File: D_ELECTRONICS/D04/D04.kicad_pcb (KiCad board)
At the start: 2 copper layers, 27.9 x 48.3 mm, 22 parts, among them J0 Conn_01x01_Male, J1 Conn_01x01_Male, J2 Conn_01x01_Male, J3 Conn_01x01_Male, J4 Conn_01x03_Female, J5 Conn_01x04_Female, K1 G5LE-1, Q1 MMBT3904, U2 LTV-817S

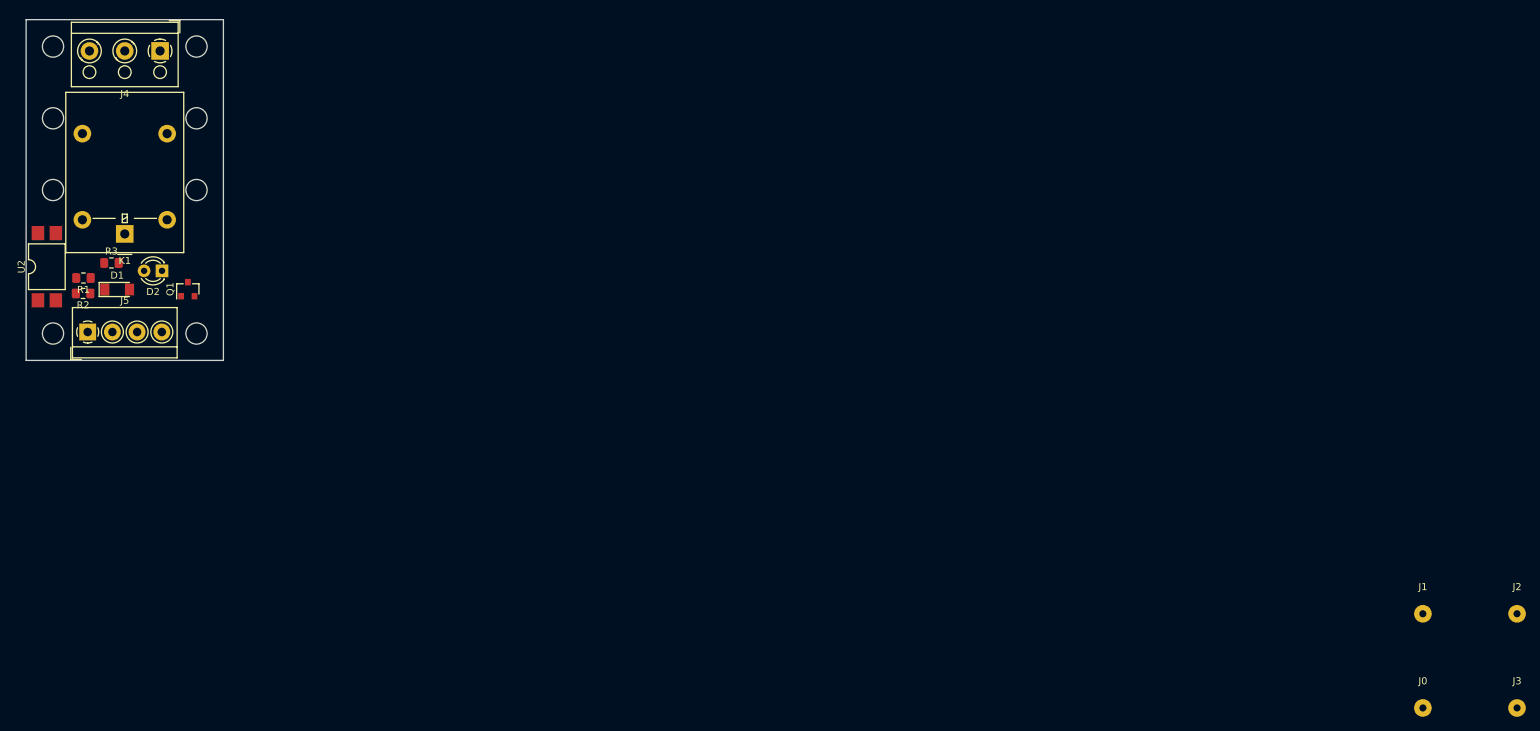
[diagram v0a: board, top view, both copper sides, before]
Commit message: all traces routed
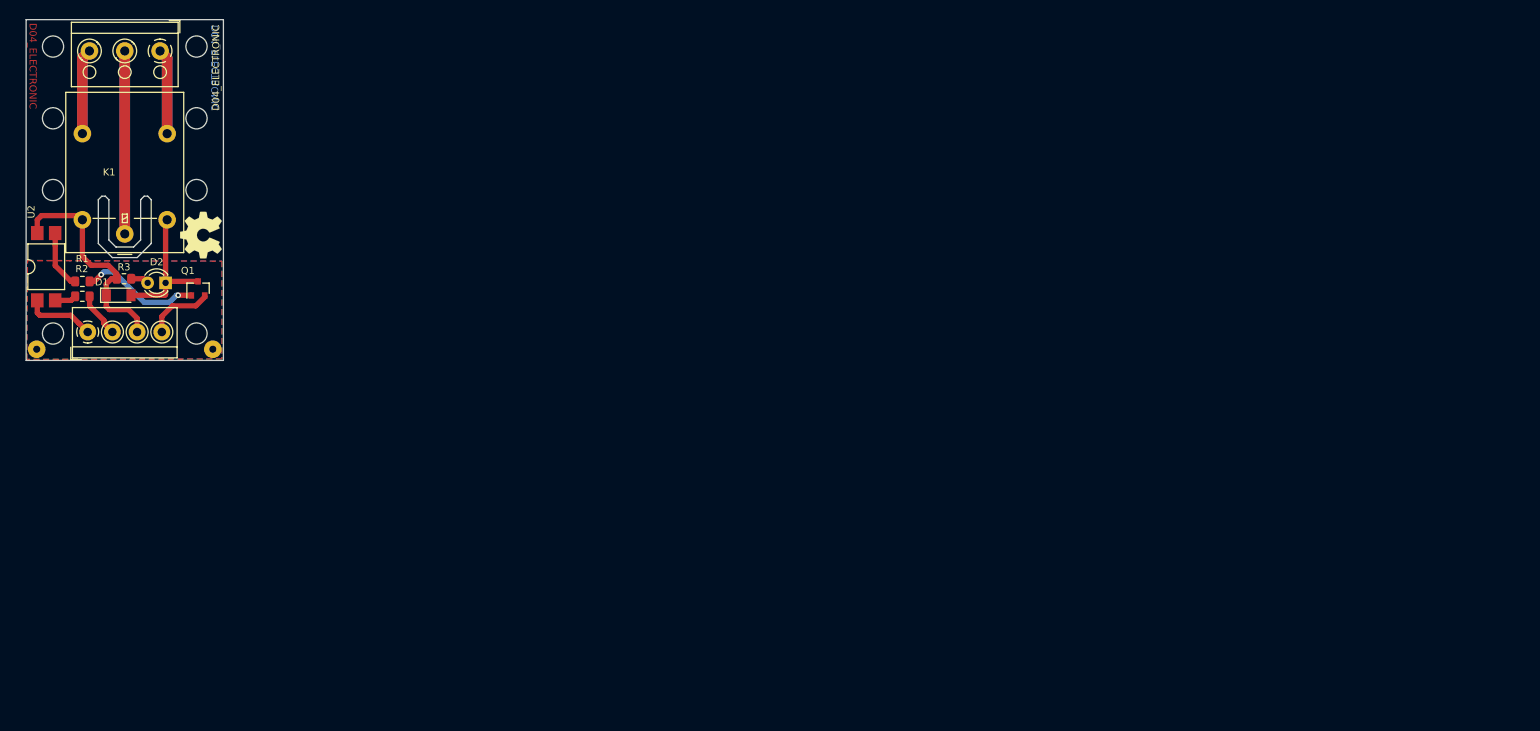
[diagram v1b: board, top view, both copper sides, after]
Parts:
- removed J2, J3: Conn_01x01_Male, Connector_Wire:SolderWirePad_1x01_Drill1mm
- added REF**: OSHW-Symbol_6.7x6mm_SilkScreen, Symbol:OSHW-Symbol_6.7x6mm_SilkScreen, B.Cu at (23.6, 54.3)
- added REF**: OSHW-Symbol_6.7x6mm_SilkScreen, Symbol:OSHW-Symbol_6.7x6mm_SilkScreen, F.Cu at (44.8, 50.5)
- moved J0 202.8 mm to (21.5, 66.7), turned to 45 degrees
- moved J1 175.4 mm to (46.4, 66.7), turned to 45 degrees
- moved R3 2.86 mm to (33.9, 56.7)
- moved D2 1.78 mm to (39.8, 57.3)
- moved Q1 1.45 mm to (44.3, 58.1)
- moved D1 0.84 mm to (33.1, 59.0)
- moved R1 0.51 mm to (28.0, 57.1)
- moved R2 0.42 mm to (28.0, 59.2)
- moved U2 0.09 mm to (22.9, 55.0)
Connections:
- J5 pad 1: Net-(D1-Pad1) -> Net-(J5-Pad1)
- J5 pad 3: Net-(J5-Pad3) -> Net-(D1-Pad1)
- R2 pad 1: Net-(R2-Pad1) -> Net-(J5-Pad2)
- U2 pad 1: Net-(R2-Pad2) -> Net-(J5-Pad1)
- U2 pad 2: Net-(U2-Pad2) -> Net-(R2-Pad2)
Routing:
- net Net-(J4-Pad2): track 0.00 -> 51.8 mm
- net Net-(D1-Pad1): track 0.00 -> 32.5 mm
- net Net-(J4-Pad3): track 0.00 -> 24.2 mm
- net Net-(J4-Pad1): track 0.00 -> 24.2 mm
- net Net-(D1-Pad2): track 0.00 -> 20.3 mm
- net Net-(Q1-Pad1): track 0.00 -> 17.2 mm, vias 0 -> 2
- net Net-(J5-Pad1): track 0.00 -> 10.0 mm
- net Net-(J5-Pad4): track 0.00 -> 9.64 mm
- net Net-(R1-Pad2): track 0.00 -> 8.35 mm
- net Net-(J5-Pad2): track 0.00 -> 6.39 mm
- net Net-(R2-Pad2): track 0.00 -> 3.06 mm
- net Net-(D2-Pad2): track 0.00 -> 2.57 mm
- added copper zone on B.Cu, net Net-(J0-Pad1)
- added copper zone on F.Cu, net Net-(J0-Pad1)
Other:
- outline, holes or cut-outs redrawn
- board text added: "D04_ELECTRONIC"
- board text added: "GND VCC IN- IN+"
